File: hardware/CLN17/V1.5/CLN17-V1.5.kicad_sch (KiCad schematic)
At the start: 104 parts, among them IC1 STM32G431CB, J1 PWR, J2 PWR, J3 TYPE-C-31-M-12, J4 Motor, J5 CTRL, J6 CAN, J7 CAN, J8 DEBUG, J9 IO, Q1 AO3401, SW1 SW_Push, SW2 SW_Push, U1 TMC2209, U10 H5VU25U, U2 TLE5012B, U4 XC6206, U5 H5VU25U, U8 TJA1042, U9 LGS5148, Y1 12M

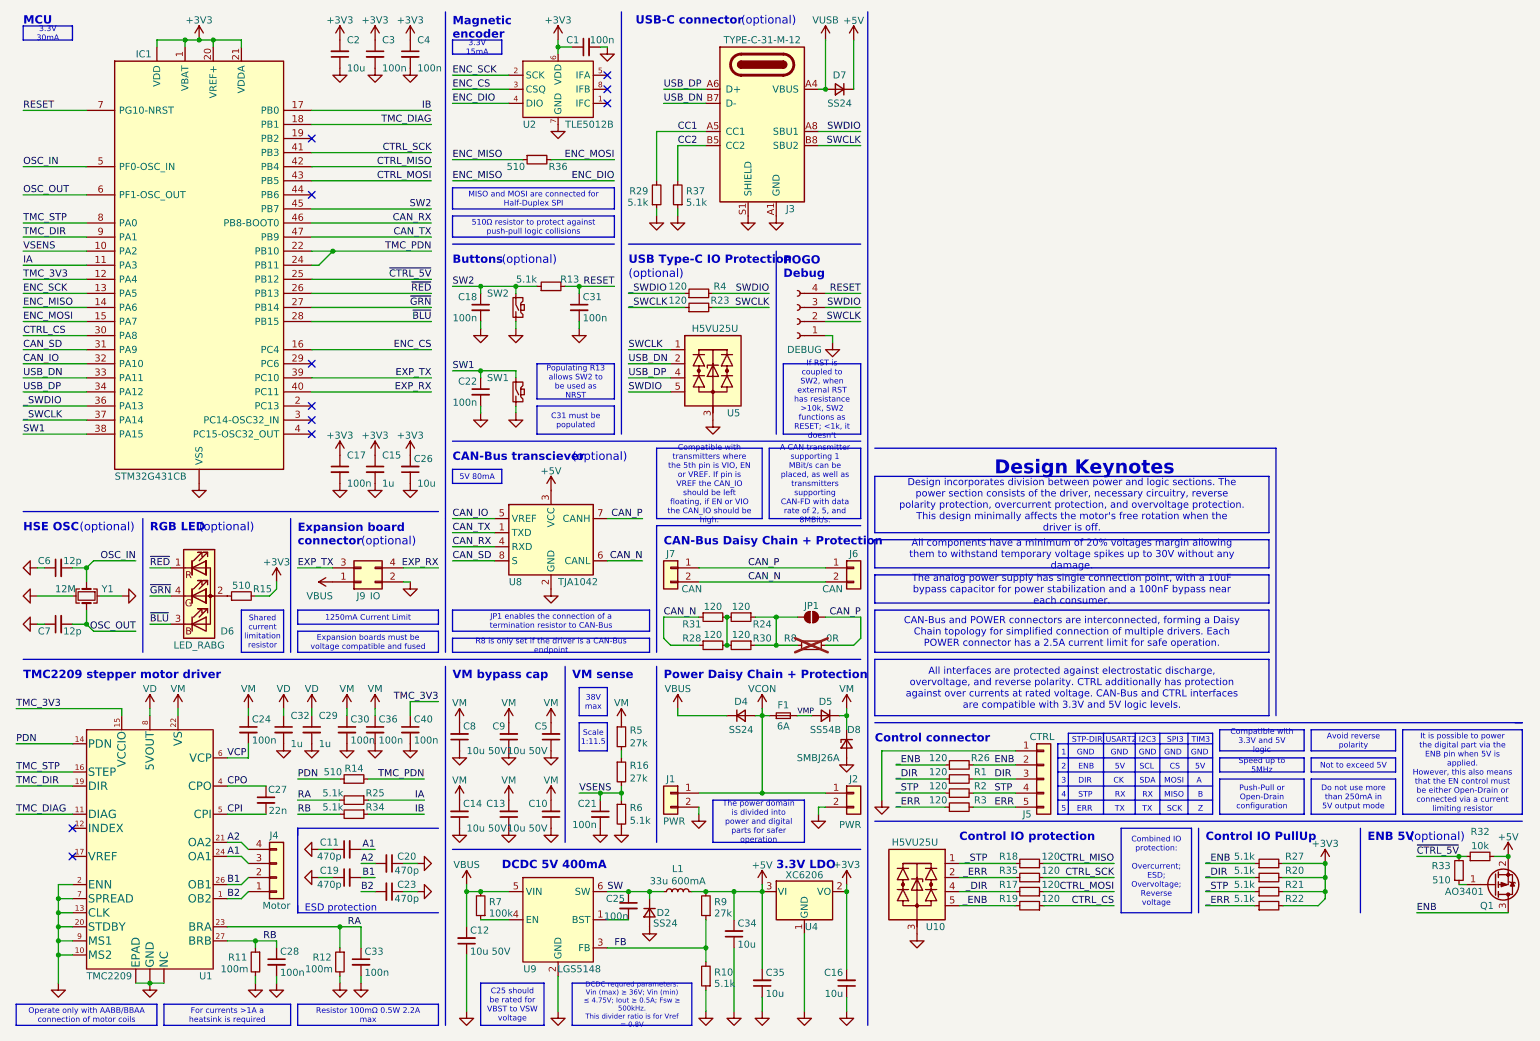
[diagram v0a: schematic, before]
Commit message: CLN17 V1.5 design improvements
- Removed CAN-bus termination resistor [the termination resistor will be integrated into the wire to avoid mix-ups]
- Replaced LDO with a less noisy one, noise reduction improved from 50db@1kHz to 70db@1kHz [noise reduction]
- Added pull-up to ground on PC6, PC13, PC14, PC15 [software version detection]
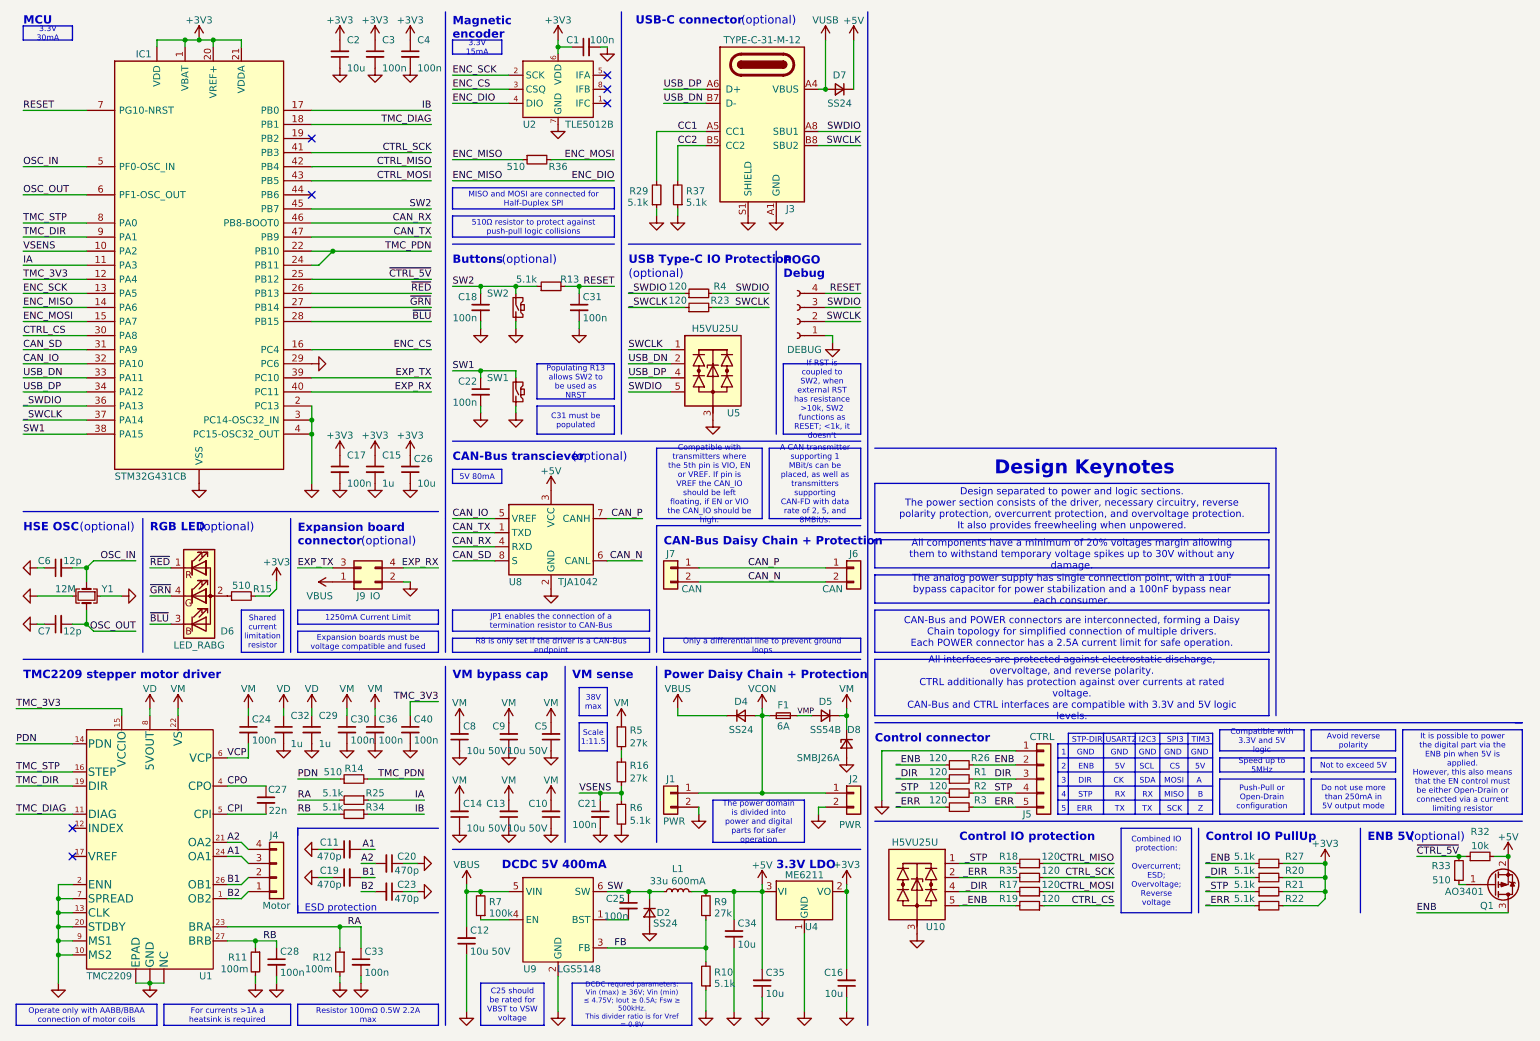
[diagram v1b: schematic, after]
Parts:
- removed JP1: SolderJumper_2_Open, FP_lib:SolderJumper, symbol SolderJumper_2_Open
- removed R24, R28, R30, R31: 120, FP_lib:R0402, symbol R_Small
- removed R8: 0R, FP_lib:R0402, symbol R_Small
- U4: value XC6206 -> ME6211; LCSC Part # C5446 -> C168807
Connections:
- net GND: now also IC1.2 (PC13), IC1.29 (PC6), IC1.3 (PC14-OSC32_IN), IC1.4 (PC15-OSC32_OUT)
- no-connect marks 11 -> 7
